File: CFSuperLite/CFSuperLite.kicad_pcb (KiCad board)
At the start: 2 copper layers, 99.9 x 99.9 mm, 23 parts, among them J1 IDE_CONNECTOR, J2 CF Adapter Power, J3 Bus_ISA_8bit, SW1 Options, U1 BIOS FLASH, U2 74HCT245, U3 ATF/GAL16V8x-15, U4 DS1315, Y1 32.768 KHz

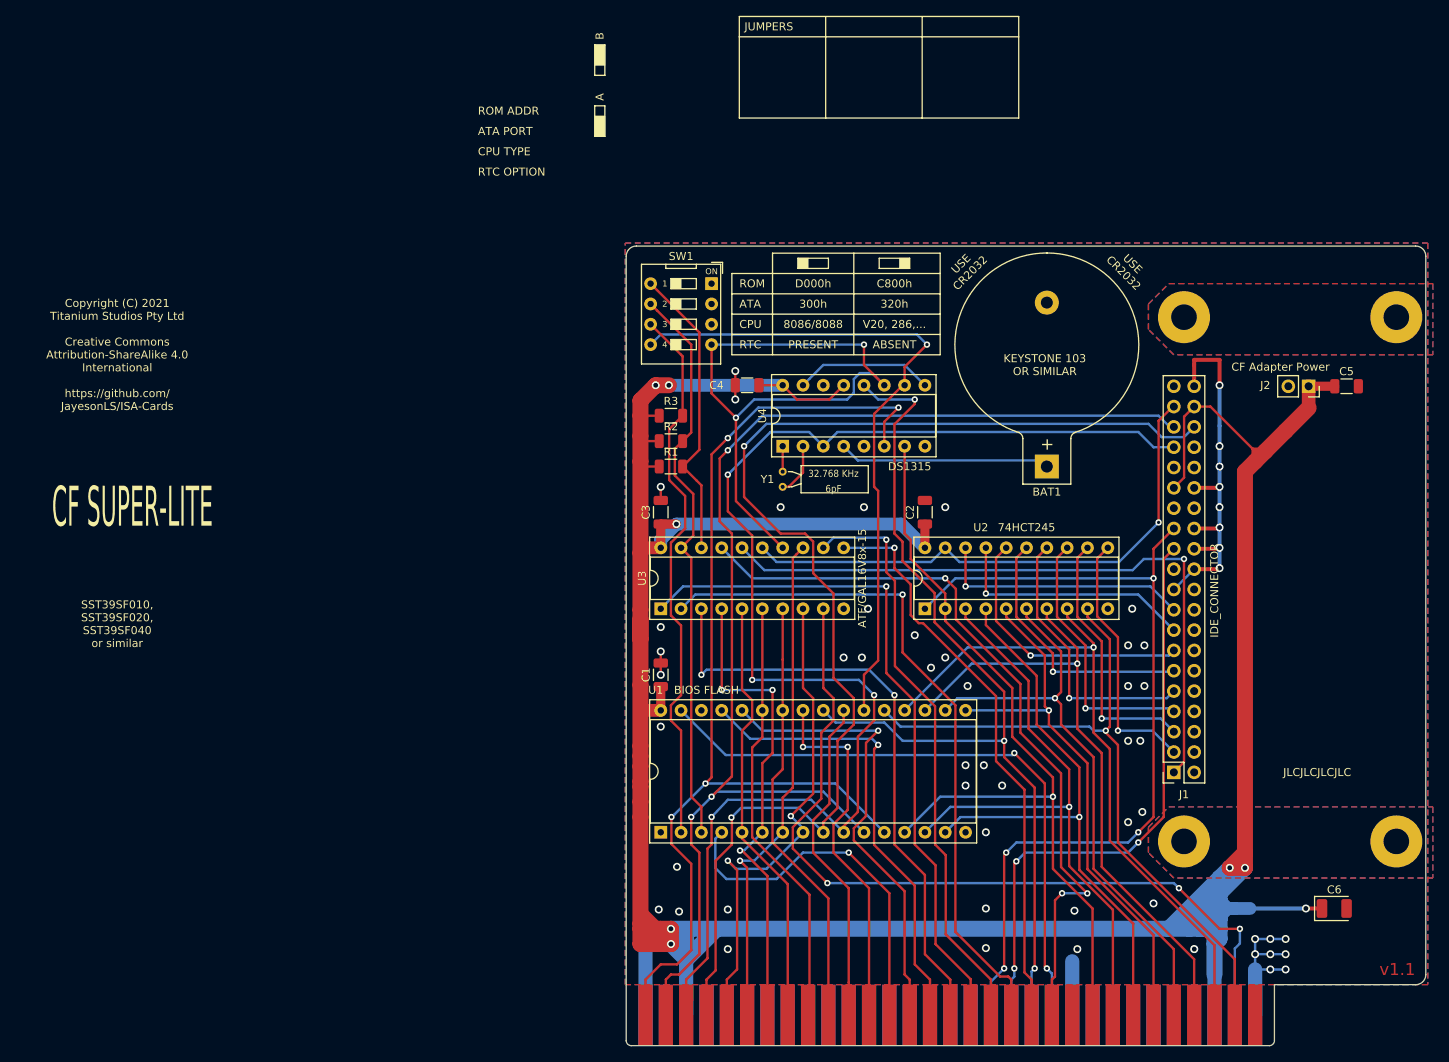
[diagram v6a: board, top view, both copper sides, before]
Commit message: CFSuperLite: Finished first pass on layout.
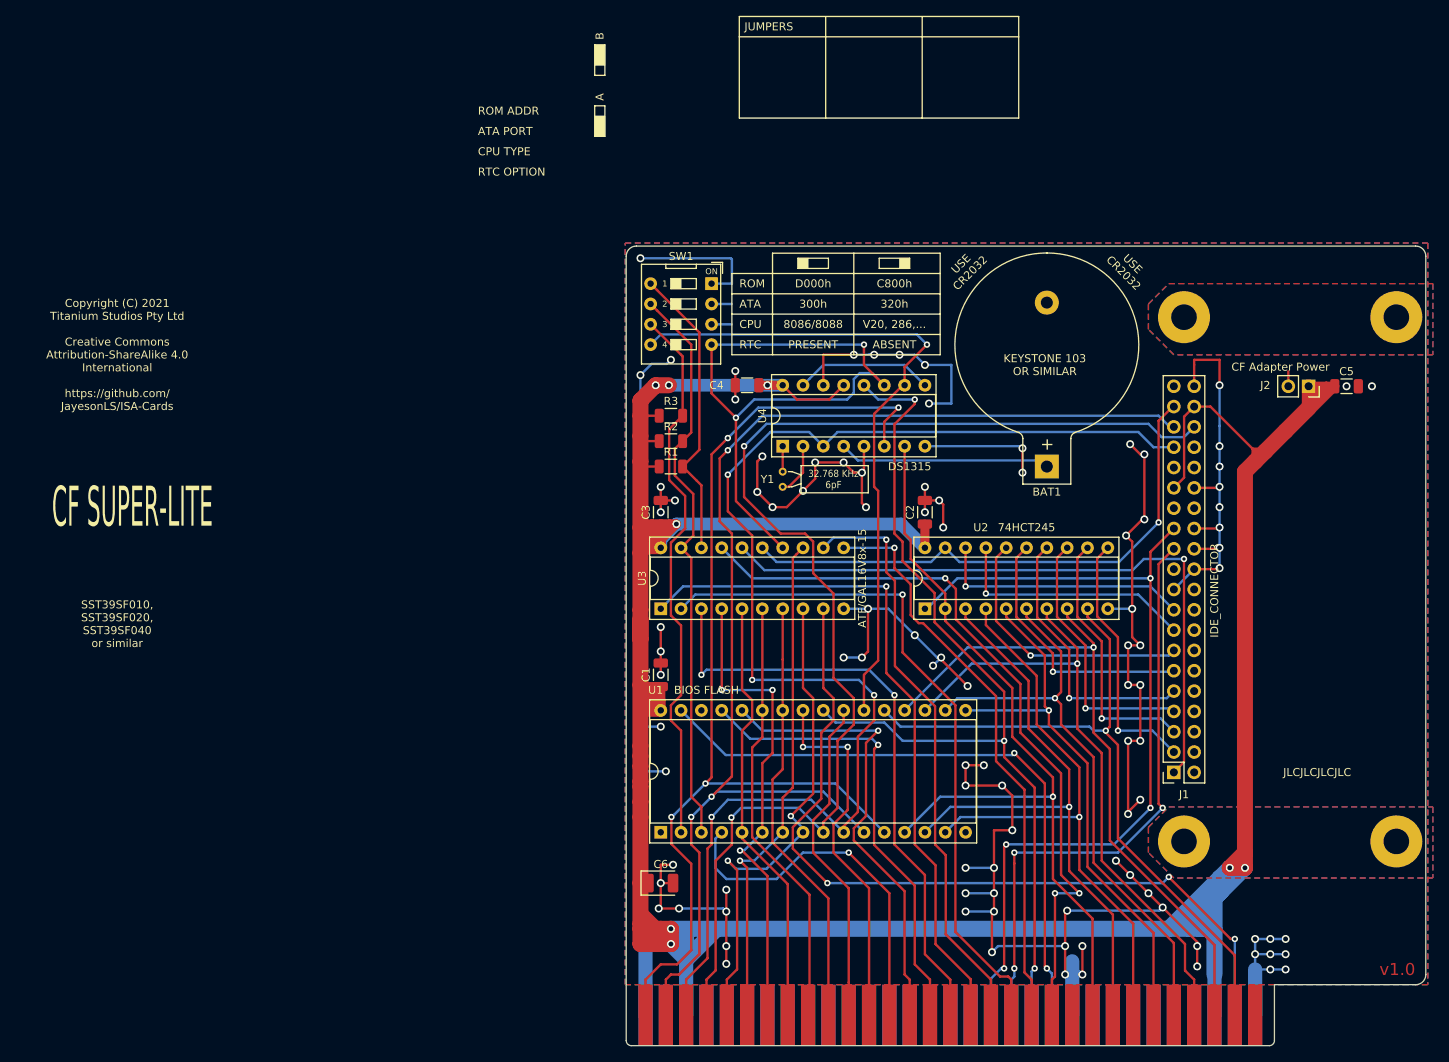
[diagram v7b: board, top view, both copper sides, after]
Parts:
- moved C6 84.2 mm to (101.0, 121.9)
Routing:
- net GND: track 158.8 -> 501.1 mm, vias 58 -> 101
- net VCC: track 452.3 -> 460.4 mm
- net RESET: track 103.7 -> 102.7 mm
- net AEN: track 95.2 -> 94.3 mm
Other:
- board text added: "Thanks to the XTIDE Universal BIOS Team and others who contributed to the XTIDE Universal BIOS. Additional thanks to Rob Krenicki, Jacob Dorne/Monotech PCs, James Pearce/Lo-tech and Derek Osborn for their influencing works."
- board text added: "v1.0"
- board text removed: "Thanks to the XTIDE Universal BIOS Team and others who contributed to the XTIDE Universal BIOS. Additional thanks to Rob Krenicki, Jacob Dorne/Monotech PCs and James Pearce/Lo-tech for their influencing works."
- board text removed: "v1.1"

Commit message: CFSuperLite: Complete first pass on silkscreen. Board is complete.
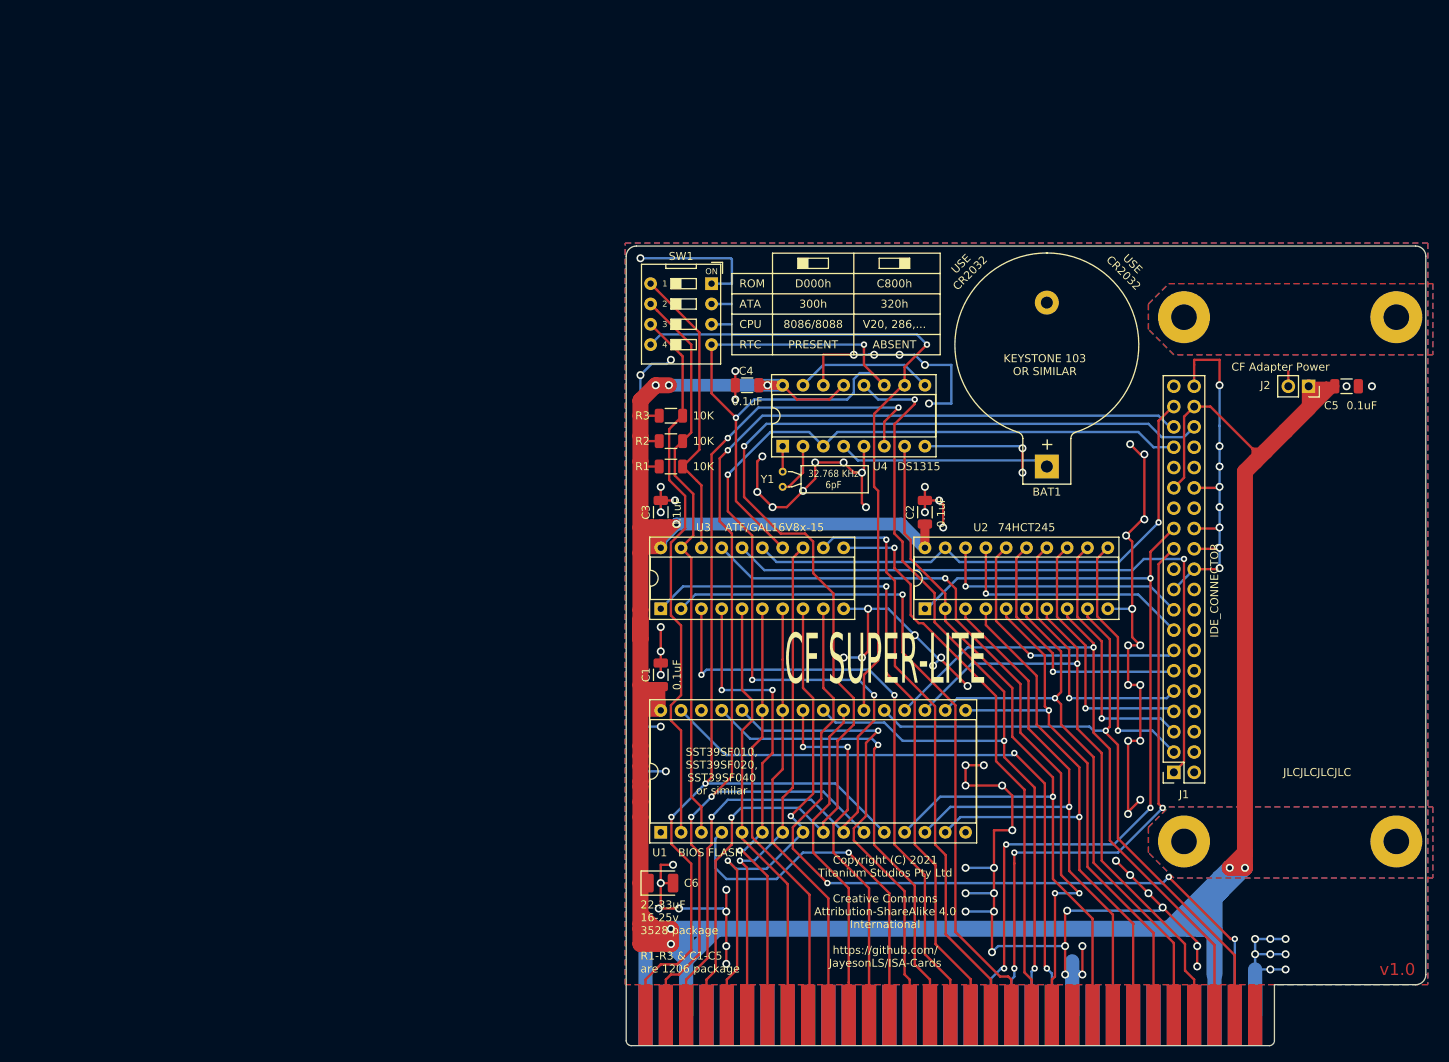
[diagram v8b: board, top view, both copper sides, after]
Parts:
- C6: value 22uF-33uF 16-25v -> 22-44uF 16-25v
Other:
- board text added: "22-33uF 16-25v 3528 package"
- board text added: "R1-R3 & C1-C5 are 1206 package"
- board text removed: "A"
- board text removed: "ATA PORT"
- board text removed: "B"
- board text removed: "CPU TYPE"
- board text removed: "JUMPERS"
- board text removed: "ROM ADDR"
- board text removed: "RTC OPTION"
